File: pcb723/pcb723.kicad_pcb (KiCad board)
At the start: 4 copper layers, 90 x 70 mm, 71 parts, among them J1 Conn_01x02_Pin, J10 Conn_01x05_Socket, J11 Conn_01x05_Socket, J2 Conn_01x02_Pin, J3 Conn_02x07_Odd_Even, J4 Conn_02x02_Odd_Even, J5 USB_C_Receptacle_USB2.0_16P, J6 Conn_02x13_Odd_Even, J7 Conn_02x14_Odd_Even, J8 Conn_02x13_Odd_Even, J9 Conn_02x12_Odd_Even, SW1 SW_Push, U1 STM32H723ZGT6, U2 AMS1117-3.3, Y1 8MHz 20pF

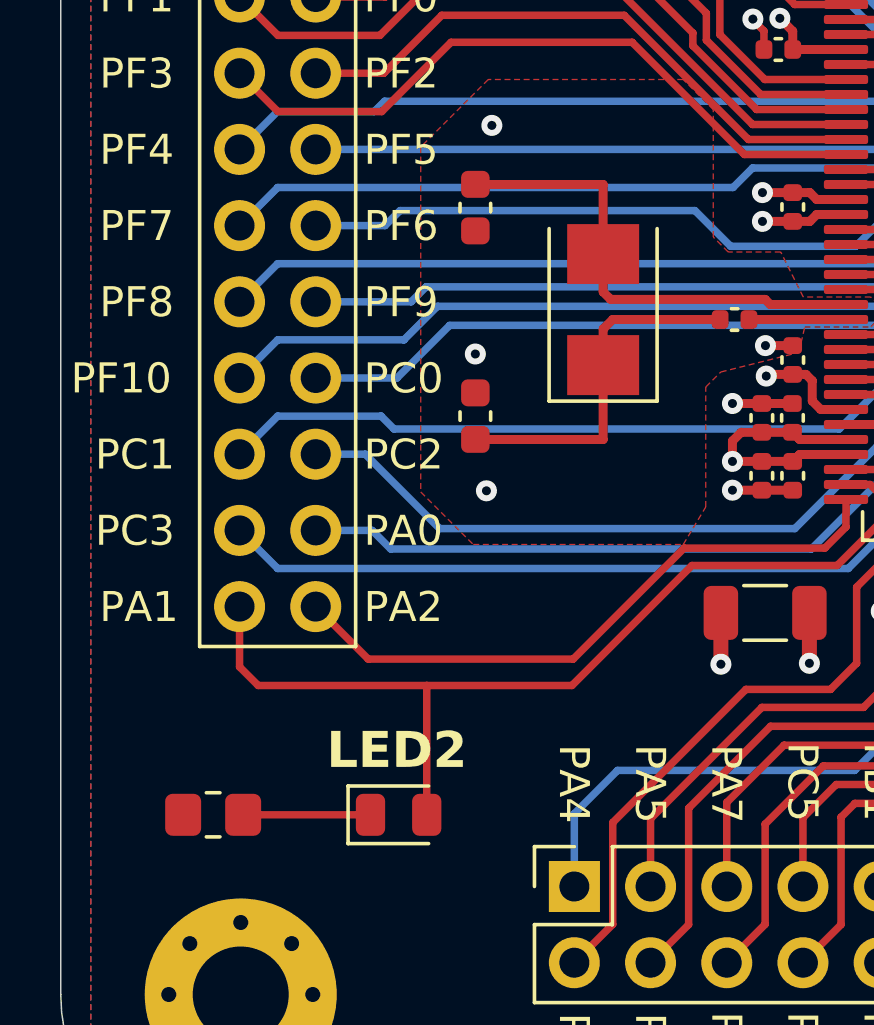
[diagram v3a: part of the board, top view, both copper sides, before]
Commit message: Crystal 3D model
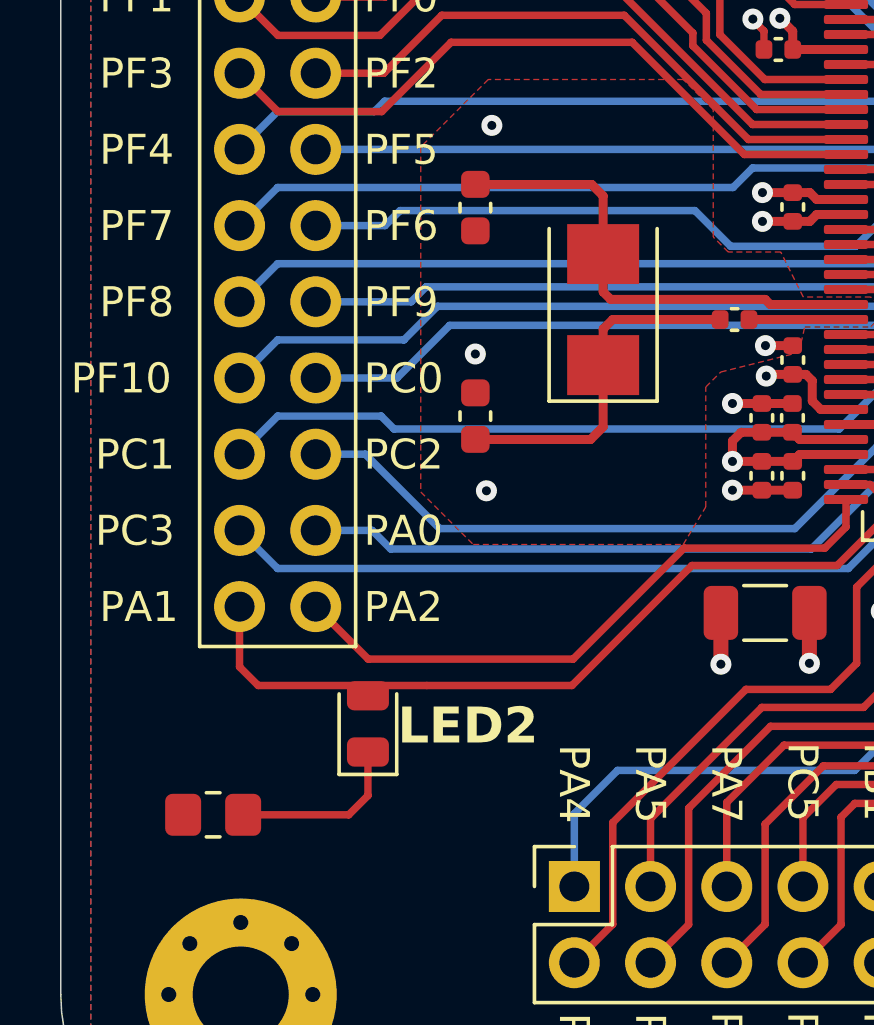
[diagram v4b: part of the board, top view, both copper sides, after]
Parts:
- moved D3 3.20 mm to (100.2, 95.0), turned to 90 degrees
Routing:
- net /PA1: track 32.3 -> 28.0 mm
- net Net-(D3-K): track 4.25 -> 5.88 mm
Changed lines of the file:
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@@
 	(footprint "LED_SMD:LED_0805_2012Metric"
 		(layer "F.Cu")
-		(at 101.2625 98.01)
+		(at 100.24 94.98 90)
 		(descr "LED SMD 0805 (2012 Metric), square (rectangular) end terminal, IPC_7351 nominal, (Body size source: https://docs.google.com/spreadsheets/d/1BsfQQcO9C6DZCsRaXUlFlo91Tg2WpOkGARC1WS5S8t0/edit?usp=sharing), generated with kicad-footprint-generator")
 		(tags "LED")
 		(property "Reference" "D3"
-			(at 0 -1.65 0)
+			(at 0 -1.65 270)
 			(layer "F.SilkS")
 			(hide yes)
@@
 		)
 		(property "Value" "Red"
-			(at 0 1.65 0)
+			(at 0 1.65 270)
 			(layer "F.Fab")
 			(hide yes)
@@
 		)
 		(property "Footprint" "LED_SMD:LED_0805_2012Metric"
-			(at 0 0 0)
+			(at 0 0 90)
 			(unlocked yes)
 			(layer "F.Fab")
@@
 		)
 		(property "Datasheet" ""
-			(at 0 0 0)
+			(at 0 0 90)
 			(unlocked yes)
 			(layer "F.Fab")
@@
 		)
 		(property "Description" "Light emitting diode"
-			(at 0 0 0)
+			(at 0 0 90)
 			(unlocked yes)
 			(layer "F.Fab")
@@
 		)
 		(property "JLC#" "C84256"
-			(at 0 0 0)
+			(at 0 0 90)
 			(unlocked yes)
 			(layer "F.Fab")
@@
 		(attr smd)
 		(fp_line
-			(start -1.685 -0.96)
-			(end -1.685 0.96)
+			(start 1 -0.96)
+			(end -1.685 -0.96)
 			(stroke
 				(width 0.12)
@@
 		)
 		(fp_line
-			(start -1.685 0.96)
-			(end 1 0.96)
+			(start -1.685 -0.96)
+			(end -1.685 0.96)
 			(stroke
 				(width 0.12)
@@
 		)
 		(fp_line
-			(start 1 -0.96)
-			(end -1.685 -0.96)
+			(start -1.685 0.96)
+			(end 1 0.96)
 			(stroke
 				(width 0.12)
@@
 		)
 		(fp_line
-			(start -1.68 -0.95)
-			(end 1.68 -0.95)
+			(start 1.68 -0.95)
+			(end 1.68 0.95)
 			(stroke
 				(width 0.05)
@@
 		)
 		(fp_line
-			(start -1.68 0.95)
-			(end -1.68 -0.95)
+			(start -1.68 -0.95)
+			(end 1.68 -0.95)
 			(stroke
 				(width 0.05)
@@
 		)
 		(fp_line
-			(start 1.68 -0.95)
-			(end 1.68 0.95)
+			(start 1.68 0.95)
+			(end -1.68 0.95)
 			(stroke
 				(width 0.05)
@@
 		)
 		(fp_line
-			(start 1.68 0.95)
-			(end -1.68 0.95)
+			(start -1.68 0.95)
+			(end -1.68 -0.95)
 			(stroke
 				(width 0.05)
@@
 		)
 		(fp_line
-			(start -1 -0.3)
-			(end -1 0.6)
+			(start 1 -0.6)
+			(end -0.7 -0.6)
 			(stroke
 				(width 0.1)
@@
 		)
 		(fp_line
-			(start -1 0.6)
-			(end 1 0.6)
+			(start -0.7 -0.6)
+			(end -1 -0.3)
 			(stroke
 				(width 0.1)
@@
 		)
 		(fp_line
-			(start -0.7 -0.6)
-			(end -1 -0.3)
+			(start -1 -0.3)
+			(end -1 0.6)
 			(stroke
 				(width 0.1)
@@
 		)
 		(fp_line
-			(start 1 -0.6)
-			(end -0.7 -0.6)
+			(start 1 0.6)
+			(end 1 -0.6)
 			(stroke
 				(width 0.1)
@@
 		)
 		(fp_line
-			(start 1 0.6)
-			(end 1 -0.6)
+			(start -1 0.6)
+			(end 1 0.6)
 			(stroke
 				(width 0.1)
@@
 		)
 		(fp_text user "${REFERENCE}"
-			(at 0 0 0)
+			(at 0 0 270)
 			(layer "F.Fab")
 			(effects
@@
 		)
 		(pad "1" smd roundrect
-			(at -0.9375 0)
+			(at -0.9375 0 90)
 			(size 0.975 1.4)
 			(layers "F.Cu" "F.Paste" "F.Mask")
@@
 		)
 		(pad "2" smd roundrect
-			(at 0.9375 0)
+			(at 0.9375 0 90)
 			(size 0.975 1.4)
 			(layers "F.Cu" "F.Paste" "F.Mask")
@@
 		)
 		(model "${KICAD8_3DMODEL_DIR}/Crystal.3dshapes/Crystal_SMD_5032-2Pin_5.0x3.2mm.wrl"
+			(hide yes)
 			(offset
 				(xyz 0 0 0)
@@
 			)
 		)
+		(model "${KICAD8_3DMODEL_DIR}/Crystal.3dshapes/Crystal_SMD_0603-2Pin_6.0x3.5mm.wrl"
+			(offset
+				(xyz 0 0 0)
+			)
+			(scale
+				(xyz 0.92 1 1)
+			)
+			(rotate
+				(xyz 0 0 0)
+			)
+		)
 	)
 	(footprint "MountingHole:MountingHole_3.2mm_M3_Pad_Via"
@@
 	)
 	(gr_text "LED2"
-		(at 98.8625 96.56 0)
+		(at 101.23 95.747 0)
 		(layer "F.SilkS")
 		(effects
@@
 	)
 	(segment
-		(start 108.08 81.82)
-		(end 108.4 81.5)
+		(start 103.82 85.495)
+		(end 103.825 85.5)
 		(width 0.3)
 		(layer "F.Cu")
@@
 	(segment
 		(start 103.825 85.5)
-		(end 108.08 85.5)
+		(end 107.66 85.5)
 		(width 0.3)
 		(layer "F.Cu")
@@
 	)
 	(segment
-		(start 108.4 81.5)
-		(end 111.98 81.5)
+		(start 108.08 85.08)
+		(end 108.08 81.82)
 		(width 0.3)
 		(layer "F.Cu")
@@
 	)
 	(segment
-		(start 108.08 85.5)
-		(end 108.08 81.82)
+		(start 107.66 85.5)
+		(end 108.08 85.08)
 		(width 0.3)
 		(layer "F.Cu")
@@
 	)
 	(segment
-		(start 103.82 85.495)
-		(end 103.825 85.5)
+		(start 108.08 81.82)
+		(end 108.4 81.5)
+		(width 0.3)
+		(layer "F.Cu")
+		(net 6)
+	)
+	(segment
+		(start 108.4 81.5)
+		(end 111.98 81.5)
 		(width 0.3)
 		(layer "F.Cu")
@@
 	)
 	(segment
-		(start 108.08 77)
+		(start 113.48 80.83)
+		(end 108.33 80.83)
+		(width 0.3)
+		(layer "F.Cu")
+		(net 14)
+	)
+	(segment
+		(start 107.7 77)
 		(end 103.825 77)
 		(width 0.3)
@@
 	)
 	(segment
-		(start 108.33 80.83)
-		(end 108.08 80.58)
+		(start 116.175 81)
+		(end 113.65 81)
 		(width 0.3)
 		(layer "F.Cu")
@@
 	)
 	(segment
-		(start 113.65 81)
-		(end 113.48 80.83)
+		(start 108.08 77.38)
+		(end 107.7 77)
 		(width 0.3)
 		(layer "F.Cu")
@@
 	)
 	(segment
-		(start 113.48 80.83)
-		(end 108.33 80.83)
+		(start 103.825 77)
+		(end 103.82 76.995)
 		(width 0.3)
 		(layer "F.Cu")
@@
 	)
 	(segment
-		(start 108.08 80.58)
-		(end 108.08 77)
+		(start 108.33 80.83)
+		(end 108.08 80.58)
 		(width 0.3)
 		(layer "F.Cu")
@@
 	)
 	(segment
-		(start 103.825 77)
-		(end 103.82 76.995)
+		(start 113.65 81)
+		(end 113.48 80.83)
 		(width 0.3)
 		(layer "F.Cu")
@@
 	)
 	(segment
-		(start 116.175 81)
-		(end 113.65 81)
+		(start 108.08 80.58)
+		(end 108.08 77.38)
 		(width 0.3)
 		(layer "F.Cu")
@@
 	)
 	(segment
-		(start 100.325 98.01)
-		(end 96.08 98.01)
+		(start 100.24 97.37)
+		(end 100.24 95.9175)
+		(width 0.25)
+		(layer "F.Cu")
+		(net 15)
+	)
+	(segment
+		(start 99.6 98.01)
+		(end 100.24 97.37)
+		(width 0.25)
+		(layer "F.Cu")
+		(net 15)
+	)
+	(segment
+		(start 96.08 98.01)
+		(end 99.6 98.01)
 		(width 0.25)
 		(layer "F.Cu")
@@
 		(width 0.25)
 		(layer "F.Cu")
-		(net 119)
-	)
-	(segment
-		(start 102.2 98.01)
-		(end 102.2 93.7)
-		(width 0.25)
-		(layer "F.Cu")

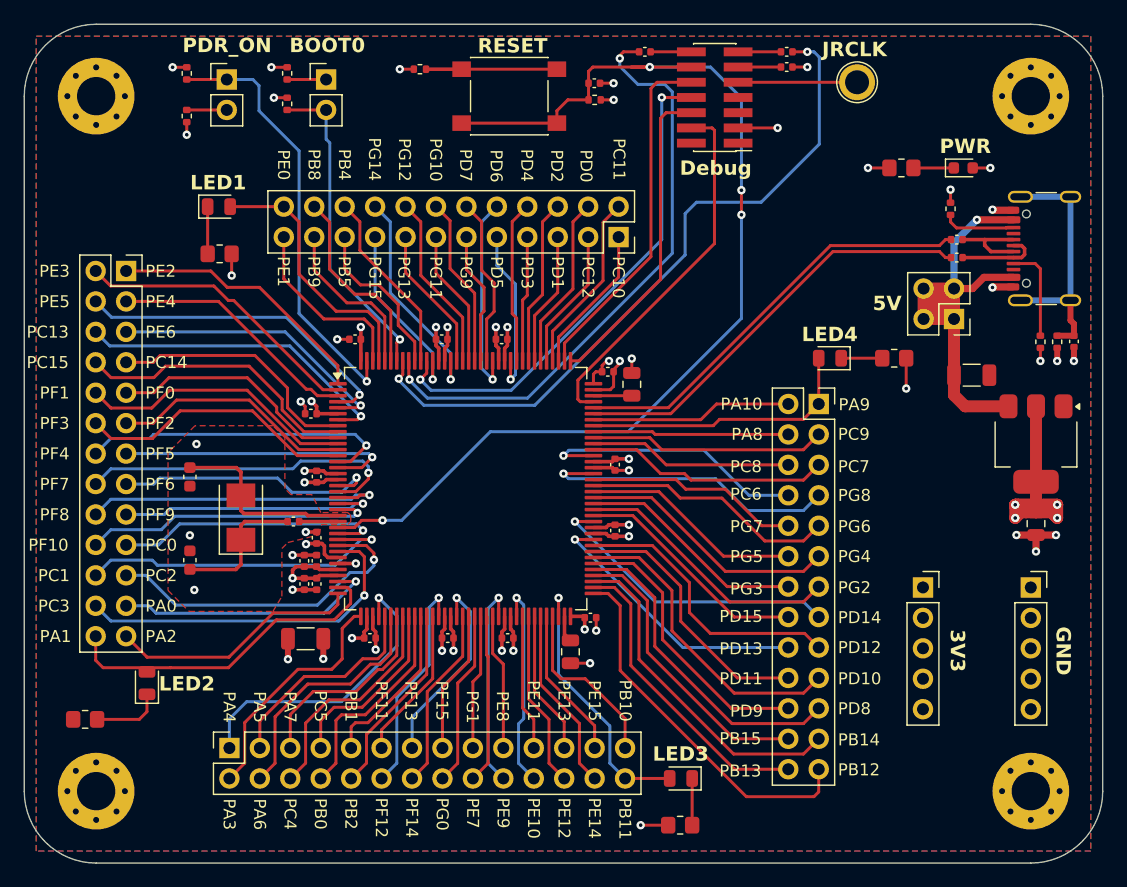
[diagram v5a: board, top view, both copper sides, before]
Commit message: Update resistor footprints
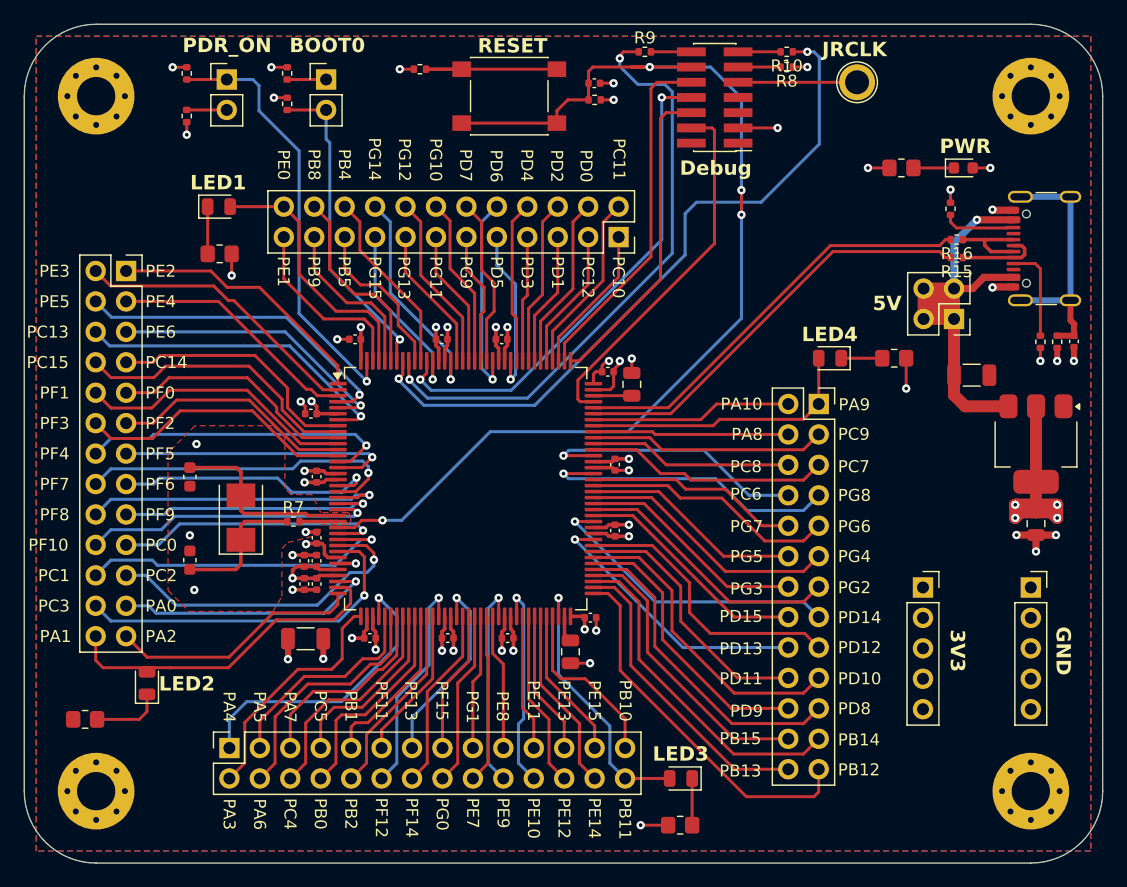
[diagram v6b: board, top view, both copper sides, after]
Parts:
- R10, R15, R16, R7, R8, R9: footprint Capacitor_SMD:C_0402_1005Metric -> Resistor_SMD:R_0402_1005Metric
